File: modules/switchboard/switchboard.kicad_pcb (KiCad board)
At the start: 2 copper layers, 71.8 x 72.3 mm, 18 parts, among them J10 Conn_C, J11 Conn_C, J12 Conn_D, J13 Conn_D, J14 Conn_Power2, J5 Conn_Power1, J6 Conn_A, J7 Conn_B, J8 Conn_B, J9 Conn_A

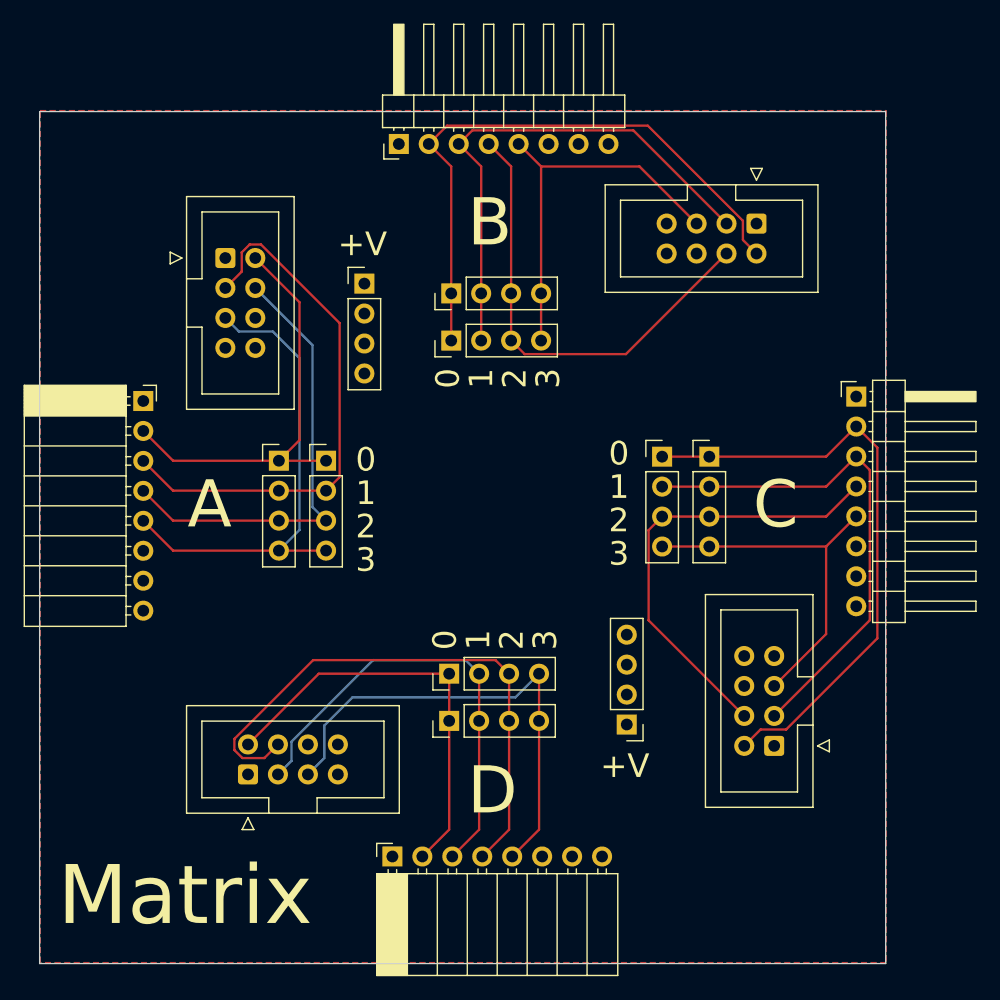
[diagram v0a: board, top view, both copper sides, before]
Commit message: Added new switchboard
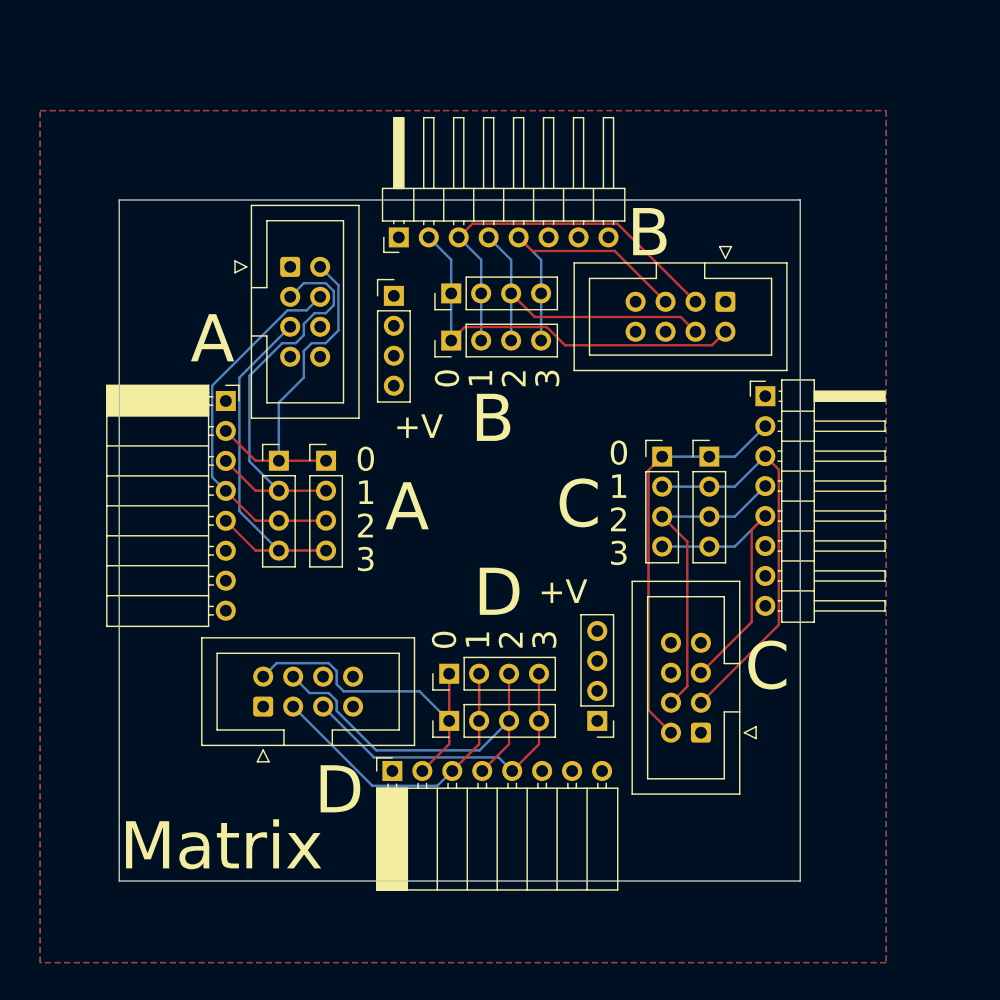
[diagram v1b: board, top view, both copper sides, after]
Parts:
- moved J3 7.92 mm to (142.7, 78.8)
- moved J15 7.71 mm to (173.8, 92.2)
- moved J17 7.25 mm to (142.1, 124.0)
- moved J4 7.13 mm to (170.4, 84.2)
- moved J1 7.00 mm to (128.0, 92.6)
- moved J16 6.31 mm to (168.3, 120.8)
- moved J18 5.89 mm to (131.2, 118.5)
- moved J2 5.55 mm to (133.5, 81.2)
- moved J14 2.71 mm to (142.2, 83.7)
- moved J5 2.52 mm to (159.5, 119.8)
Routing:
- net Net-(J3-D0): track 51.3 -> 34.4 mm
- net Net-(J10-Pin_1): track 51.3 -> 34.5 mm
- net Net-(J12-Pin_3): track 48.4 -> 31.6 mm
- net Net-(J12-Pin_4): track 41.2 -> 27.5 mm
- net Net-(J3-D2): track 39.7 -> 26.5 mm
- net Net-(J12-Pin_2): track 38.9 -> 26.0 mm
- net Net-(J10-Pin_3): track 38.3 -> 27.1 mm
- net Net-(J3-D1): track 43.9 -> 32.8 mm
- net Net-(J1-D1): track 46.2 -> 36.1 mm
- net Net-(J1-D3): track 41.3 -> 31.7 mm
- net Net-(J10-Pin_2): track 43.4 -> 33.9 mm
- net Net-(J3-D3): track 32.7 -> 24.3 mm
- net Net-(J12-Pin_1): track 36.0 -> 28.1 mm
- net Net-(J1-D2): track 38.8 -> 31.2 mm
- net Net-(J1-D0): track 36.0 -> 29.4 mm
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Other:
- board size 71.8 x 72.3 mm -> 57.8 x 57.8 mm
